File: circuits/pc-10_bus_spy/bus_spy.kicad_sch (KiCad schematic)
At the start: 91 parts, among them Q1 2N7002, Q10 2N7002, Q11 2N7002, Q12 2N7002, Q13 2N7002, Q14 2N7002, Q15 2N7002, Q16 2N7002, Q17 2N7002, Q18 2N7002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

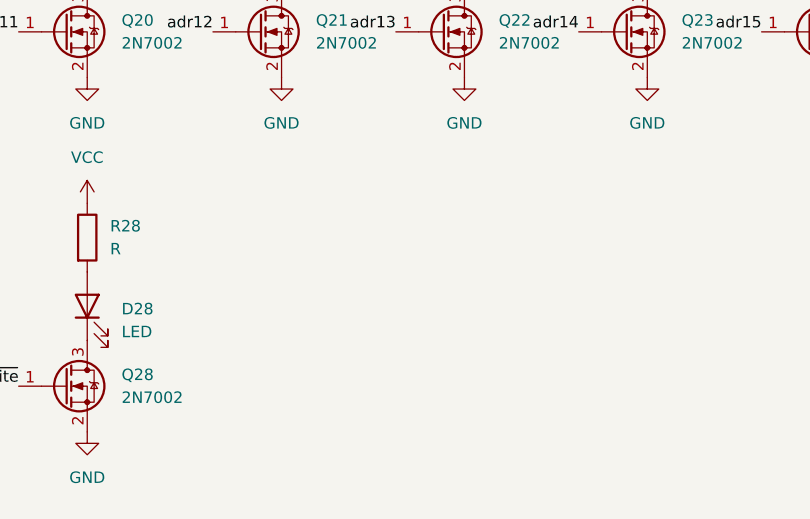
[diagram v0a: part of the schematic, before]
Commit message: add filter and decoupling capacitors to all boards
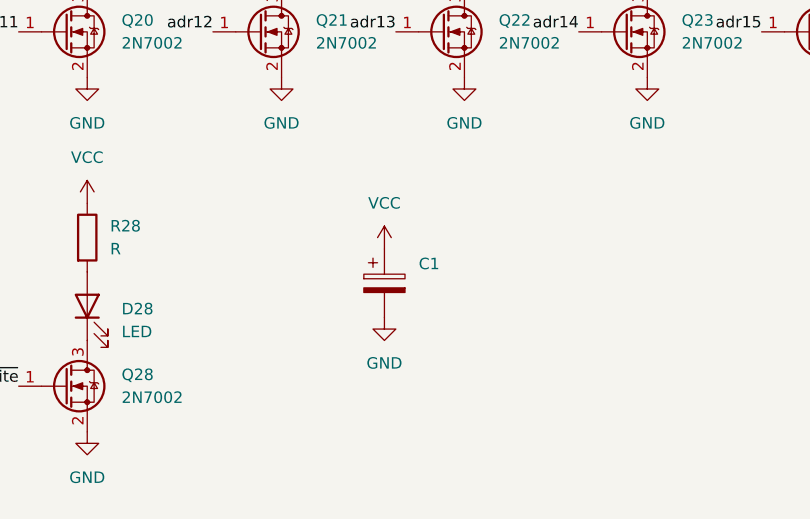
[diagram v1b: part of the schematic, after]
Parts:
- added C1: C_Polarized, Capacitor_SMD:CP_Elec_5x5.3, symbol Device:C_Polarized
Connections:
- net GND: now also C1.2
- net VCC: now also C1.1
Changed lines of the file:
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@@
+	)
+	(symbol
+		(lib_id "power:VCC")
+		(at 157.48 151.13 0)
+		(unit 1)
+		(exclude_from_sim no)
+		(in_bom yes)
+		(on_board yes)
+		(dnp no)
+		(fields_autoplaced yes)
+		(property "Reference" "#PWR019"
+			(at 157.48 154.94 0)
+			(effects
+				(font
+					(size 1.27 1.27)
+				)
+				(hide yes)
+			)
+		)
+		(property "Value" "VCC"
+			(at 157.48 146.05 0)
+			(effects
+				(font
+					(size 1.27 1.27)
+				)
+			)
+		)
+		(property "Footprint" ""
+			(at 157.48 151.13 0)
+			(effects
+				(font
+					(size 1.27 1.27)
+				)
+				(hide yes)
+			)
+		)
+		(property "Datasheet" ""
+			(at 157.48 151.13 0)
+			(effects
+				(font
+					(size 1.27 1.27)
+				)
+				(hide yes)
+			)
+		)
+		(property "Description" "Power symbol creates a global label with name \"VCC\""
+			(at 157.48 151.13 0)
+			(effects
+				(font
+					(size 1.27 1.27)
+				)
+				(hide yes)
+			)
+		)
+		(pin "1"
+		)
+		(instances
+			(project "bus_spy"
+				(path "/41a1e4f1-e027-482a-b298-2d9f17a2c0a5"
+					(reference "#PWR019")
+					(unit 1)
+				)
+			)
+		)
 	)
 	(symbol
@@
 	)
 	(symbol
+		(lib_id "power:GND")
+		(at 157.48 158.75 0)
+		(unit 1)
+		(exclude_from_sim no)
+		(in_bom yes)
+		(on_board yes)
+		(dnp no)
+		(fields_autoplaced yes)
+		(property "Reference" "#PWR018"
+			(at 157.48 165.1 0)
+			(effects
+				(font
+					(size 1.27 1.27)
+				)
+				(hide yes)
+			)
+		)
+		(property "Value" "GND"
+			(at 157.48 163.83 0)
+			(effects
+				(font
+					(size 1.27 1.27)
+				)
+			)
+		)
+		(property "Footprint" ""
+			(at 157.48 158.75 0)
+			(effects
+				(font
+					(size 1.27 1.27)
+				)
+				(hide yes)
+			)
+		)
+		(property "Datasheet" ""
+			(at 157.48 158.75 0)
+			(effects
+				(font
+					(size 1.27 1.27)
+				)
+				(hide yes)
+			)
+		)
+		(property "Description" "Power symbol creates a global label with name \"GND\" , ground"
+			(at 157.48 158.75 0)
+			(effects
+				(font
+					(size 1.27 1.27)
+				)
+				(hide yes)
+			)
+		)
+		(pin "1"
+		)
+		(instances
+			(project "bus_spy"
+				(path "/41a1e4f1-e027-482a-b298-2d9f17a2c0a5"
+					(reference "#PWR018")
+					(unit 1)
+				)
+			)
+		)
+	)
+	(symbol
 		(lib_id "Device:R")
 		(at 166.37 27.94 0)
@@
 					(unit 1)
 				)
+			)
+		)
+	)
+	(symbol
+		(lib_id "Device:C_Polarized")
+		(at 157.48 154.94 0)
+		(unit 1)
+		(exclude_from_sim no)
+		(in_bom yes)
+		(on_board yes)
+		(dnp no)
+		(fields_autoplaced yes)
+		(property "Reference" "C1"
+			(at 161.29 152.7809 0)
+			(effects
+				(font
+					(size 1.27 1.27)
+				)
+				(justify left)
+			)
+		)
+		(property "Value" "C_Polarized"
+			(at 161.29 155.3209 0)
+			(effects
+				(font
+					(size 1.27 1.27)
+				)
+				(justify left)
+				(hide yes)
+			)
+		)
+		(property "Footprint" "Capacitor_SMD:CP_Elec_5x5.3"
+			(at 158.4452 158.75 0)
+			(effects
+				(font
+					(size 1.27 1.27)
+				)
+				(hide yes)
+			)
+		)
+		(property "Datasheet" "~"
+			(at 157.48 154.94 0)
+			(effects
+				(font
+					(size 1.27 1.27)
+				)
+				(hide yes)
+			)
+		)
+		(property "Description" "Polarized capacitor"
+			(at 157.48 154.94 0)
+			(effects
+				(font
+					(size 1.27 1.27)
+				)
+				(hide yes)
+			)
+		)
+		(pin "2"
+		)
+		(pin "1"
+		)
+		(instances
+			(project "bus_spy"
+				(path "/41a1e4f1-e027-482a-b298-2d9f17a2c0a5"
+					(reference "C1")
+					(unit 1)
+				)
